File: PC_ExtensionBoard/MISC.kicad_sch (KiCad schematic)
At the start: 11 parts, among them Q7 BSS138-7-F, Q8 BSS138-7-F

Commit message: components placement R1
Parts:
- added C103, C104, C107, C108, C112, C113, C114, C16, C17: C_100n_0402, antmicro-footprints:C_0402_1005Metric, symbol antmicroCapacitors0402:C_100n_0402
- added C106, C111: C_22u_16V_0603, antmicro-footprints:C_0603_1608Metric, symbol antmicroCapacitors0603:C_22u_16V_0603
- added C109, C110: C_100n_0402, PC_Components_1:C_0402_1005Metric, symbol antmicroCapacitors0402:C_100n_0402
- added J2: Conn_01x04_Pin, Connector_Hirose:Hirose_DF13-04P-1.25DSA_1x04_P1.25mm_Vertical, symbol Connector:Conn_01x04_Pin
- added R178, R192, R193, R194, R195, R238, R239, R240, R241, R242, R243, R244, R245, R314, R315, R316, R317: R_0R_0402, antmicro-footprints:R_0402_1005Metric, symbol antmicroResistors0402:R_0R_0402
- added R182, R183, R184, R185, R186, R187, R188, R189, R190: R_1k_0402, antmicro-footprints:R_0402_1005Metric, symbol antmicroResistors0402:R_1k_0402
- added R191: R_1k_0402, PC_Components_1:R_0402_1005Metric, symbol antmicroResistors0402:R_1k_0402
- added TP44, TP45, TP46, TP47, TP48: TP_0.75mm_SMD, antmicro-footprints:TP_SMD_0.75mm, symbol antmicroTestPoints:TP_0.75mm_SMD
- added U37: 9DBL0651CKILF, antmicro-footprints:VFQFPN-40-1EP_5x5mm_P0.4mm_EP3.5x3.5mm, symbol antmicroClockTimingClockGeneratorsPLLsFrequencySynthesizers:9DBL0651CKILF
- added U38: 74AUP2G132, PC_Components_1:VSSOP-8_2.3x2mm_P0.5mm, symbol antmicroLogicGatesandInverters:74AUP2G132
- added U4: STM32G0B1RCT6, PC_ExtensionBoard:LQFP-64_L10.0-W10.0-P0.50-LS12.0-BL, symbol MCU_ST_STM32G0:STM32G0B1RCTx
- added Y1: Oscillator_32.768kHz_ECS_2520MV, PC_Components_1:Oscillator_SMD_ECS_2520MV_2.5x2mm, symbol antmicroOscillators:Oscillator_32.768kHz_ECS_2520MV
- D17, D18: footprint antmicro-footprints:PLCC4_3.2x2.8mm -> PC_Components_1:PLCC4_3.2x2.8mm
- Q7, Q8: footprint antmicro-footprints:SOT-23-3 -> PC_Components_1:SOT-23-3
- R140, R141, R142, R152, R153: footprint antmicro-footprints:R_0402_1005Metric -> PC_Components_1:R_0402_1005Metric
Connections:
- net GND: now also C103.1, C104.1, C106.1, C107.1, C108.1, C109.1, C110.1, C111.1, C112.1, C113.1, C114.1, C16.1, C17.1, R182.2, R183.2, R184.2, R185.2, R186.2, R188.2, U37.41 (EPAD), U37.8 (GNDDIG), U38.4 (GND), U38.5 (2A), U38.6 (2B), U4.9 (VSS), Y1.2 (GND)
- net LED_B: now also U4.56 (PD6)
- net LED_G: now also U4.40 (PD8)
- net LED_R: now also U4.41 (PD9)
- net PWR_OK: now also U4.55 (PD5)
- new net: R245.1, U4.13 (PC0)
- new net: R178.2, R182.1, U37.13 (~{OE0})
- new net: R185.1, R316.2, U37.29 (~{OE3})
- new net: R189.1, U37.38 (~{OE5})
- new net: R184.1, R315.2, U37.24 (~{OE2})
- new net: TP44.1, U37.9 (SCLK)
- new net: R244.1, U4.14 (PC1)
- new net: R190.1, U37.40 (~{CKPWRGD_PD})
- new net: R183.1, R314.2, U37.21 (~{OE1})
- new net: R186.1, R317.2, U37.35 (~{OE4})
- new net: R187.2, R188.1, U37.2 (~{HIBW_BYPM_LOBW})
- new net: TP45.1, U37.10 (SDAT)
- new net: R191.1, Y1.1 (EN)
- new net: TP46.1, U37.1 (SADR_{TRI})
- new net: R243.1, U4.15 (PC2)
- new net: R239.1, U4.38 (PC6)
- new net: R240.1, U4.26 (PC5)
- new net: U38.1 (1A), U38.2 (1B), Y1.3 (OUT)
- new net: R242.1, U4.16 (PC3)
- new net: R238.1, U4.39 (PC7)
- new net: R241.1, U4.25 (PC4)
- new net +3V3: C103.2, C104.2, C106.2, C107.2, C108.2, C109.2, C110.2, C111.2, C112.2, C113.2, C114.2, C16.2, C17.2, R187.1, R189.2, R190.2, R191.2, U37.11 (VDDDIG3V3), U37.12 (VDDIO), U37.16 (VDD3V3), U37.17 (VDDIO), U37.25 (VDDA3V3), U37.26 (VDDIO), U37.31 (VDD3V3), U37.32 (VDDIO), U37.39 (VDDIO), U37.5 (VDDR), U38.8 (VCC), U4.6 (VBAT), U4.8 (VDD), Y1.4 (VDD)
- new net DIF0+: R192.1, U37.14 (DIF0+)
- new net DIF0-: R193.1, U37.15 (DIF0-)
- new net DIF1+: R194.1, U37.18 (DIF1+)
- new net DIF1-: R195.1, U37.19 (DIF1-)
- new net DIF5+: TP47.1, U37.36 (DIF5+)
- new net DIF5-: TP48.1, U37.37 (DIF5-)
- new net GPIOEX0: R238.2
- new net GPIOEX1: R239.2
- new net GPIOEX2: R240.2
- new net GPIOEX3: R241.2
- new net GPIOEX4: R242.2
- new net GPIOEX5: R243.2
- new net GPIOEX6: R244.2
- new net GPIOEX7: R245.2
- new net MCU_SWCLK: J2.3 (Pin_3), U4.46 (PA14)
- new net MCU_SWDIO: J2.4 (Pin_4), U4.45 (PA13)
- new net MCU_USB_D+: U4.44 (PA10/PA12)
- new net MCU_USB_D-: U4.43 (PA9/PA11)
- new net PCIE_{REF0}.CK+: R192.2
- new net PCIE_{REF0}.CK-: R193.2
- new net PCIE_{REF3}.CK+: R195.2
- new net PCIE_{REF3}.CK-: R194.2
- new net PCIE_{REFIN}.CK+: U37.6 (CLK_IN+)
- new net PCIE_{REFIN}.CK-: U37.7 (CLK_IN-)
- new net SUSCLK: U38.7 (1Y)
- new net ~{CLKREQ0}: R178.1
- new net ~{CLKREQ1}: R317.1
- new net ~{CLKREQ2}: R315.1
- new net ~{CLKREQ3}: R314.1
- new net ~{CLKREQ4}: R316.1
- no-connect marks 1 -> 8
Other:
- note added: "PCIe clock fanout buffer"
- note added: "SUSCLK generator"

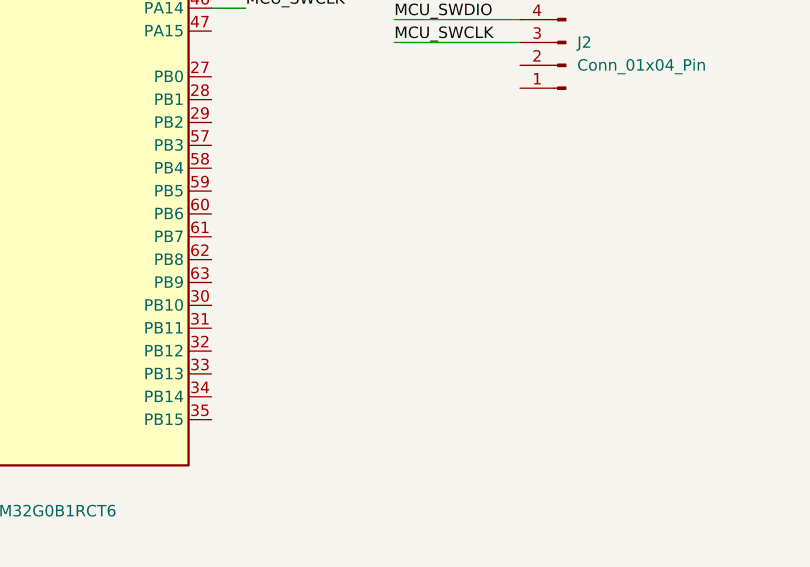
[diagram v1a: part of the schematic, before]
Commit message: update schematic
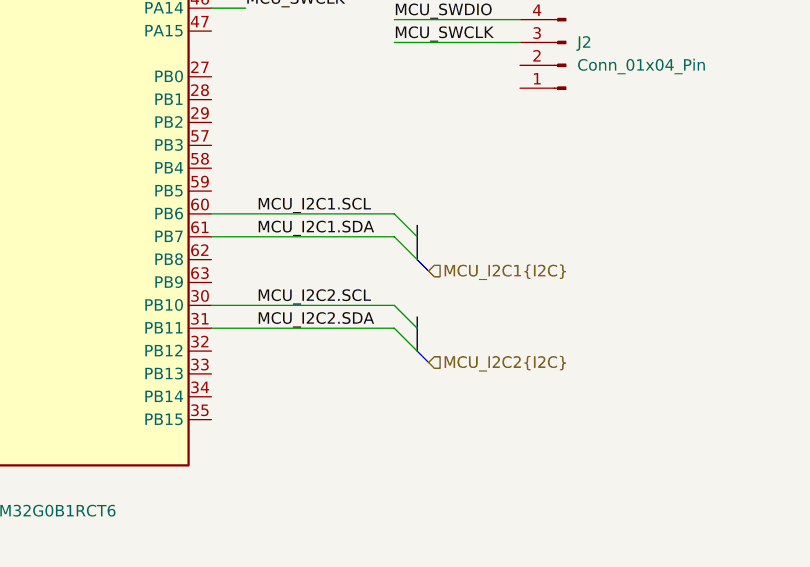
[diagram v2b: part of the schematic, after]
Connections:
- net MCU_I2C2.SCL: now reaches U4.30 (PB10)
- net MCU_I2C2.SDA: now reaches U4.31 (PB11)
- net MCU_I2C1.SCL: now reaches U4.60 (PB6)
- net MCU_I2C1.SDA: now reaches U4.61 (PB7)
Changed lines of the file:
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@@
+	)
+	(bus_entry
+		(at 283.21 118.11)
+		(size 2.54 2.54)
+		(stroke
+			(width 0)
+			(type default)
+		)
+	)
+	(bus_entry
+		(at 283.21 115.57)
+		(size 2.54 2.54)
+		(stroke
+			(width 0)
+			(type default)
+		)
 	)
 	(bus_entry
@@
 	)
 	(bus_entry
+		(at 283.21 105.41)
+		(size 2.54 2.54)
+		(stroke
+			(width 0)
+			(type default)
+		)
+	)
+	(bus_entry
 		(at 698.5 72.39)
 		(size 1.27 1.27)
@@
 		)
 	)
+	(bus_entry
+		(at 283.21 107.95)
+		(size 2.54 2.54)
+		(stroke
+			(width 0)
+			(type default)
+		)
+	)
 	(wire
 		(pts
@@
 		)
 	)
+	(bus
+		(pts
+			(xy 287.02 121.92) (xy 285.75 120.65)
+		)
+		(stroke
+			(width 0)
+			(type default)
+		)
+	)
 	(wire
 		(pts
@@
 	(wire
 		(pts
+			(xy 262.89 115.57) (xy 283.21 115.57)
+		)
+		(stroke
+			(width 0)
+			(type default)
+		)
+	)
+	(wire
+		(pts
 			(xy 577.85 115.57) (xy 577.85 114.3)
 		)
@@
 		)
 	)
+	(bus
+		(pts
+			(xy 285.75 106.68) (xy 285.75 107.95)
+		)
+		(stroke
+			(width 0)
+			(type default)
+		)
+	)
 	(wire
 		(pts
@@
 		)
 	)
+	(bus
+		(pts
+			(xy 285.75 107.95) (xy 285.75 110.49)
+		)
+		(stroke
+			(width 0)
+			(type default)
+		)
+	)
 	(wire
 		(pts
@@
 		)
 	)
+	(bus
+		(pts
+			(xy 285.75 118.11) (xy 285.75 120.65)
+		)
+		(stroke
+			(width 0)
+			(type default)
+		)
+	)
 	(wire
 		(pts
@@
 	(wire
 		(pts
+			(xy 262.89 107.95) (xy 283.21 107.95)
+		)
+		(stroke
+			(width 0)
+			(type default)
+		)
+	)
+	(wire
+		(pts
 			(xy 608.33 85.09) (xy 608.33 100.33)
 		)
@@
 		)
 	)
+	(bus
+		(pts
+			(xy 287.02 111.76) (xy 285.75 110.49)
+		)
+		(stroke
+			(width 0)
+			(type default)
+		)
+	)
 	(wire
 		(pts
@@
 		)
 	)
+	(bus
+		(pts
+			(xy 285.75 116.84) (xy 285.75 118.11)
+		)
+		(stroke
+			(width 0)
+			(type default)
+		)
+	)
 	(wire
 		(pts
@@
 		(pts
 			(xy 213.36 34.29) (xy 224.79 34.29)
+		)
+		(stroke
+			(width 0)
+			(type default)
+		)
+	)
+	(wire
+		(pts
+			(xy 262.89 118.11) (xy 283.21 118.11)
+		)
+		(stroke
+			(width 0)
+			(type default)
+		)
+	)
+	(wire
+		(pts
+			(xy 262.89 105.41) (xy 283.21 105.41)
 		)
 		(stroke
@@
 		)
 	)
+	(label "MCU_I2C1.SDA"
+		(at 267.97 107.95 0)
+		(effects
+			(font
+				(size 1.27 1.27)
+			)
+			(justify left bottom)
+		)
+	)
 	(label "PCIE_{REF3}.CK-"
 		(at 684.53 74.93 0)
@@
 		)
 	)
+	(label "MCU_I2C1.SCL"
+		(at 267.97 105.41 0)
+		(effects
+			(font
+				(size 1.27 1.27)
+			)
+			(justify left bottom)
+		)
+	)
 	(label "PWR_OK"
 		(at 191.77 74.93 0)
+		(effects
+			(font
+				(size 1.27 1.27)
+			)
+			(justify left bottom)
+		)
+	)
+	(label "MCU_I2C2.SCL"
+		(at 267.97 115.57 0)
+		(effects
+			(font
+				(size 1.27 1.27)
+			)
+			(justify left bottom)
+		)
+	)
+	(label "MCU_I2C2.SDA"
+		(at 267.97 118.11 0)
 		(effects
 			(font
@@
 		)
 	)
+	(hierarchical_label "MCU_I2C1{I2C}"
+		(shape input)
+		(at 287.02 111.76 0)
+		(effects
+			(font
+				(size 1.27 1.27)
+			)
+			(justify left)
+		)
+	)
 	(hierarchical_label "~{CLKREQ0}"
 		(shape input)
@@
 		)
 	)
+	(hierarchical_label "MCU_I2C2{I2C}"
+		(shape input)
+		(at 287.02 121.92 0)
+		(effects
+			(font
+				(size 1.27 1.27)
+			)
+			(justify left)
+		)
+	)

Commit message: refactor project
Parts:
- removed H4, H5: Lightpipe_Bivar_SLP3-300-250-F, antmicro-footprints:Mech_Lightpipe_Bivar_SLP3-300-250-F, symbol antmicroMechanicalParts:Lightpipe_Bivar_SLP3-300-250-F
- C103, C104, C107, C108, C109, C110, C112, C113, C114, C16, C17: symbol antmicroCapacitors0402:C_100n_0402 -> A_PC_ExtensionBoard:C_100n_0402
- C106, C111: symbol antmicroCapacitors0603:C_22u_16V_0603 -> A_PC_ExtensionBoard:C_22u_16V_0603
- D17, D18: symbol antmicroLEDIndicationDiscrete:LED_RGB_PLCC4_ASMB_MTB1_0A3A2 -> A_PC_ExtensionBoard:LED_RGB_PLCC4_ASMB_MTB1_0A3A2
- Q7, Q8: footprint PC_Components_1:SOT-23-3 -> antmicro-footprints:SOT-23-3; symbol antmicroTransistorsFETsMOSFETsSingle:BSS138-7-F -> A_PC_ExtensionBoard:BSS138-7-F
- R140, R141, R142, R152, R153: footprint PC_Components_1:R_0402_1005Metric -> antmicro-footprints:R_0402_1005Metric; symbol antmicroResistors0402:R_10k_0402 -> A_PC_ExtensionBoard:R_10k_0402; Public (none) -> False
- R178, R192, R193, R194, R195, R238, R239, R240, R241, R242, R243, R244, R245, R314, R315, R316, R317: symbol antmicroResistors0402:R_0R_0402 -> A_PC_ExtensionBoard:R_0R_0402
- R182, R183, R184, R185, R186, R187, R188, R189, R190: symbol antmicroResistors0402:R_1k_0402 -> A_PC_ExtensionBoard:R_1k_0402
- R191: footprint PC_Components_1:R_0402_1005Metric -> antmicro-footprints:R_0402_1005Metric; symbol antmicroResistors0402:R_1k_0402 -> A_PC_ExtensionBoard:R_1k_0402
- TP44, TP45, TP46, TP47, TP48: symbol antmicroTestPoints:TP_0.75mm_SMD -> A_PC_ExtensionBoard:TP_0.75mm_SMD
- U37: symbol antmicroClockTimingClockGeneratorsPLLsFrequencySynthesizers:9DBL0651CKILF -> A_PC_ExtensionBoard:9DBL0651CKILF
- U38: symbol antmicroLogicGatesandInverters:74AUP2G132 -> A_PC_ExtensionBoard:74AUP2G132
- Y1: symbol antmicroOscillators:Oscillator_32.768kHz_ECS_2520MV -> A_PC_ExtensionBoard:Oscillator_32.768kHz_ECS_2520MV
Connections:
- net +3V3 renamed +3.3V

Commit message: re-link symbol
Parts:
- C103, C104, C107, C108, C112, C113, C114, C16, C17: footprint antmicro-footprints:C_0402_1005Metric -> PC_Components_1:C_0402_1005Metric
- C106, C111: footprint antmicro-footprints:C_0603_1608Metric -> PC_Components_1:C_0603_1608Metric
- Q7, Q8: footprint antmicro-footprints:SOT-23-3 -> PC_Components_1:SOT-23-3
- R140, R141, R142, R152, R153, R178, R182, R183, R184, R185, R186, R187, R188, R189, R190, R191, R192, R193, R194, R195, R238, R239, R240, R241, R242, R243, R244, R245, R314, R315, R316, R317: footprint antmicro-footprints:R_0402_1005Metric -> PC_Components_1:R_0402_1005Metric
- TP44, TP45, TP46, TP47, TP48: footprint antmicro-footprints:TP_SMD_0.75mm -> PC_Components_1:TP_SMD_0.75mm
- U37: footprint antmicro-footprints:VFQFPN-40-1EP_5x5mm_P0.4mm_EP3.5x3.5mm -> PC_Components_1:VFQFPN-40-1EP_5x5mm_P0.4mm_EP3.5x3.5mm
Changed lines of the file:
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@@
 			)
 		)
-		(property "Footprint" "antmicro-footprints:R_0402_1005Metric"
+		(property "Footprint" "PC_Components_1:R_0402_1005Metric"
 			(at 121.92 67.31 0)
 			(hide yes)
@@
 			)
 		)
-		(property "Footprint" "antmicro-footprints:C_0402_1005Metric"
+		(property "Footprint" "PC_Components_1:C_0402_1005Metric"
 			(at 623.57 43.18 0)
 			(hide yes)
@@
 			)
 		)
-		(property "Footprint" "antmicro-footprints:R_0402_1005Metric"
+		(property "Footprint" "PC_Components_1:R_0402_1005Metric"
 			(at 175.26 72.39 0)
 			(hide yes)
@@
 			)
 		)
-		(property "Footprint" "antmicro-footprints:R_0402_1005Metric"
+		(property "Footprint" "PC_Components_1:R_0402_1005Metric"
 			(at 571.5 102.87 0)
 			(hide yes)
@@
 			)
 		)
-		(property "Footprint" "antmicro-footprints:C_0402_1005Metric"
+		(property "Footprint" "PC_Components_1:C_0402_1005Metric"
 			(at 586.74 43.18 0)
 			(hide yes)
@@
 			)
 		)
-		(property "Footprint" "antmicro-footprints:R_0402_1005Metric"
+		(property "Footprint" "PC_Components_1:R_0402_1005Metric"
 			(at 568.96 129.54 0)
 			(hide yes)
@@
 			)
 		)
-		(property "Footprint" "antmicro-footprints:R_0402_1005Metric"
+		(property "Footprint" "PC_Components_1:R_0402_1005Metric"
 			(at 598.17 85.09 0)
 			(hide yes)
@@
 			)
 		)
-		(property "Footprint" "antmicro-footprints:R_0402_1005Metric"
+		(property "Footprint" "PC_Components_1:R_0402_1005Metric"
 			(at 562.61 129.54 0)
 			(hide yes)
@@
 			)
 		)
-		(property "Footprint" "antmicro-footprints:TP_SMD_0.75mm"
+		(property "Footprint" "PC_Components_1:TP_SMD_0.75mm"
 			(at 607.695 104.14 0)
 			(hide yes)
@@
 			)
 		)
-		(property "Footprint" "antmicro-footprints:R_0402_1005Metric"
+		(property "Footprint" "PC_Components_1:R_0402_1005Metric"
 			(at 175.26 74.93 0)
 			(hide yes)
@@
 			)
 		)
-		(property "Footprint" "antmicro-footprints:R_0402_1005Metric"
+		(property "Footprint" "PC_Components_1:R_0402_1005Metric"
 			(at 76.2 67.31 0)
 			(hide yes)
@@
 			)
 		)
-		(property "Footprint" "antmicro-footprints:R_0402_1005Metric"
+		(property "Footprint" "PC_Components_1:R_0402_1005Metric"
 			(at 80.01 67.31 0)
 			(hide yes)
@@
 			)
 		)
-		(property "Footprint" "antmicro-footprints:R_0402_1005Metric"
+		(property "Footprint" "PC_Components_1:R_0402_1005Metric"
 			(at 598.17 87.63 0)
 			(hide yes)
@@
 			)
 		)
-		(property "Footprint" "antmicro-footprints:R_0402_1005Metric"
+		(property "Footprint" "PC_Components_1:R_0402_1005Metric"
 			(at 689.61 87.63 0)
 			(hide yes)
@@
 			)
 		)
-		(property "Footprint" "antmicro-footprints:R_0402_1005Metric"
+		(property "Footprint" "PC_Components_1:R_0402_1005Metric"
 			(at 571.5 105.41 0)
 			(hide yes)
@@
 			)
 		)
-		(property "Footprint" "antmicro-footprints:R_0402_1005Metric"
+		(property "Footprint" "PC_Components_1:R_0402_1005Metric"
 			(at 571.5 113.03 0)
 			(hide yes)
@@
 			)
 		)
-		(property "Footprint" "antmicro-footprints:R_0402_1005Metric"
+		(property "Footprint" "PC_Components_1:R_0402_1005Metric"
 			(at 613.41 119.38 0)
 			(hide yes)
@@
 			)
 		)
-		(property "Footprint" "antmicro-footprints:C_0402_1005Metric"
+		(property "Footprint" "PC_Components_1:C_0402_1005Metric"
 			(at 614.68 43.18 0)
 			(hide yes)
@@
 			)
 		)
-		(property "Footprint" "antmicro-footprints:R_0402_1005Metric"
+		(property "Footprint" "PC_Components_1:R_0402_1005Metric"
 			(at 549.91 129.54 0)
 			(hide yes)
@@
 			)
 		)
-		(property "Footprint" "antmicro-footprints:TP_SMD_0.75mm"
+		(property "Footprint" "PC_Components_1:TP_SMD_0.75mm"
 			(at 607.695 106.68 0)
 			(hide yes)
@@
 			)
 		)
-		(property "Footprint" "antmicro-footprints:R_0402_1005Metric"
+		(property "Footprint" "PC_Components_1:R_0402_1005Metric"
 			(at 118.11 67.31 0)
 			(hide yes)
@@
 			)
 		)
-		(property "Footprint" "antmicro-footprints:R_0402_1005Metric"
+		(property "Footprint" "PC_Components_1:R_0402_1005Metric"
 			(at 610.87 193.04 0)
 			(hide yes)
@@
 			)
 		)
-		(property "Footprint" "antmicro-footprints:TP_SMD_0.75mm"
+		(property "Footprint" "PC_Components_1:TP_SMD_0.75mm"
 			(at 672.465 99.06 0)
 			(hide yes)
@@
 			)
 		)
-		(property "Footprint" "antmicro-footprints:C_0603_1608Metric"
+		(property "Footprint" "PC_Components_1:C_0603_1608Metric"
 			(at 233.68 44.45 0)
 			(hide yes)
@@
 			)
 		)
-		(property "Footprint" "antmicro-footprints:TP_SMD_0.75mm"
+		(property "Footprint" "PC_Components_1:TP_SMD_0.75mm"
 			(at 672.465 96.52 0)
 			(hide yes)
@@
 			)
 		)
-		(property "Footprint" "antmicro-footprints:VFQFPN-40-1EP_5x5mm_P0.4mm_EP3.5x3.5mm"
+		(property "Footprint" "PC_Components_1:VFQFPN-40-1EP_5x5mm_P0.4mm_EP3.5x3.5mm"
 			(at 668.02 77.47 0)
 			(hide yes)
@@
 			)
 		)
-		(property "Footprint" "antmicro-footprints:C_0402_1005Metric"
+		(property "Footprint" "PC_Components_1:C_0402_1005Metric"
 			(at 577.85 43.18 0)
 			(hide yes)
@@
 			)
 		)
-		(property "Footprint" "antmicro-footprints:R_0402_1005Metric"
+		(property "Footprint" "PC_Components_1:R_0402_1005Metric"
 			(at 175.26 77.47 0)
 			(hide yes)
@@
 			)
 		)
-		(property "Footprint" "antmicro-footprints:SOT-23-3"
+		(property "Footprint" "PC_Components_1:SOT-23-3"
 			(at 118.11 111.76 0)
 			(hide yes)
@@
 			)
 		)
-		(property "Footprint" "antmicro-footprints:R_0402_1005Metric"
+		(property "Footprint" "PC_Components_1:R_0402_1005Metric"
 			(at 175.26 87.63 0)
 			(hide yes)
@@
 			)
 		)
-		(property "Footprint" "antmicro-footprints:R_0402_1005Metric"
+		(property "Footprint" "PC_Components_1:R_0402_1005Metric"
 			(at 689.61 90.17 0)
 			(hide yes)
@@
 			)
 		)
-		(property "Footprint" "antmicro-footprints:SOT-23-3"
+		(property "Footprint" "PC_Components_1:SOT-23-3"
 			(at 121.92 125.73 0)
 			(hide yes)
@@
 			)
 		)
-		(property "Footprint" "antmicro-footprints:C_0402_1005Metric"
+		(property "Footprint" "PC_Components_1:C_0402_1005Metric"
 			(at 254 44.45 0)
 			(hide yes)
@@
 			)
 		)
-		(property "Footprint" "antmicro-footprints:R_0402_1005Metric"
+		(property "Footprint" "PC_Components_1:R_0402_1005Metric"
 			(at 613.41 129.54 0)
 			(hide yes)
@@
 			)
 		)
-		(property "Footprint" "antmicro-footprints:R_0402_1005Metric"
+		(property "Footprint" "PC_Components_1:R_0402_1005Metric"
 			(at 72.39 67.31 0)
 			(hide yes)
@@
 			)
 		)
-		(property "Footprint" "antmicro-footprints:C_0402_1005Metric"
+		(property "Footprint" "PC_Components_1:C_0402_1005Metric"
 			(at 224.79 44.45 0)
 			(hide yes)
@@
 			)
 		)
-		(property "Footprint" "antmicro-footprints:R_0402_1005Metric"
+		(property "Footprint" "PC_Components_1:R_0402_1005Metric"
 			(at 575.31 129.54 0)
 			(hide yes)
@@
 			)
 		)
-		(property "Footprint" "antmicro-footprints:R_0402_1005Metric"
+		(property "Footprint" "PC_Components_1:R_0402_1005Metric"
 			(at 571.5 110.49 0)
 			(hide yes)
@@
 			)
 		)
-		(property "Footprint" "antmicro-footprints:C_0603_1608Metric"
+		(property "Footprint" "PC_Components_1:C_0603_1608Metric"
 			(at 568.96 43.18 0)
 			(hide yes)
@@
 			)
 		)
-		(property "Footprint" "antmicro-footprints:R_0402_1005Metric"
+		(property "Footprint" "PC_Components_1:R_0402_1005Metric"
 			(at 571.5 107.95 0)
 			(hide yes)
@@
 			)
 		)
-		(property "Footprint" "antmicro-footprints:R_0402_1005Metric"
+		(property "Footprint" "PC_Components_1:R_0402_1005Metric"
 			(at 175.26 85.09 0)
 			(hide yes)
@@
 			)
 		)
-		(property "Footprint" "antmicro-footprints:C_0402_1005Metric"
+		(property "Footprint" "PC_Components_1:C_0402_1005Metric"
 			(at 243.84 44.45 0)
 			(hide yes)
@@
 			)
 		)
-		(property "Footprint" "antmicro-footprints:C_0402_1005Metric"
+		(property "Footprint" "PC_Components_1:C_0402_1005Metric"
 			(at 596.9 43.18 0)
 			(hide yes)
@@
 			)
 		)
-		(property "Footprint" "antmicro-footprints:R_0402_1005Metric"
+		(property "Footprint" "PC_Components_1:R_0402_1005Metric"
 			(at 175.26 80.01 0)
 			(hide yes)
@@
 			)
 		)
-		(property "Footprint" "antmicro-footprints:R_0402_1005Metric"
+		(property "Footprint" "PC_Components_1:R_0402_1005Metric"
 			(at 175.26 90.17 0)
 			(hide yes)
@@
 			)
 		)
-		(property "Footprint" "antmicro-footprints:R_0402_1005Metric"
+		(property "Footprint" "PC_Components_1:R_0402_1005Metric"
 			(at 689.61 80.01 0)
 			(hide yes)
@@
 			)
 		)
-		(property "Footprint" "antmicro-footprints:TP_SMD_0.75mm"
+		(property "Footprint" "PC_Components_1:TP_SMD_0.75mm"
 			(at 607.695 109.22 0)
 			(hide yes)
@@
 			)
 		)
-		(property "Footprint" "antmicro-footprints:R_0402_1005Metric"
+		(property "Footprint" "PC_Components_1:R_0402_1005Metric"
 			(at 556.26 129.54 0)
 			(hide yes)
@@
 			)
 		)
-		(property "Footprint" "antmicro-footprints:R_0402_1005Metric"
+		(property "Footprint" "PC_Components_1:R_0402_1005Metric"
 			(at 175.26 82.55 0)
 			(hide yes)
@@
 			)
 		)
-		(property "Footprint" "antmicro-footprints:C_0402_1005Metric"
+		(property "Footprint" "PC_Components_1:C_0402_1005Metric"
 			(at 605.79 43.18 0)
 			(hide yes)
@@
 			)
 		)
-		(property "Footprint" "antmicro-footprints:R_0402_1005Metric"
+		(property "Footprint" "PC_Components_1:R_0402_1005Metric"
 			(at 689.61 82.55 0)
 			(hide yes)
